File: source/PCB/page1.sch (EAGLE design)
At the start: 25 parts, among them J1 RJ45-MJ88-BX11-RVSL2-3420050P1, J2 CONNECTOR-HEADER-6P-3460650P1, J4 CONNECTOR-HEADER-3P-3460810P1, J5 CONNECTOR-HEADER-2X3P-3460180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, Q1 MOSFET-N-044020001, Q2 MOSFET-N-044020001, Q3 MOSFET-N-044020001, Q4 MOSFET-N-044020001, U1 ATMEGA328P-AU-1030060P1, U2 L298-1420010P1

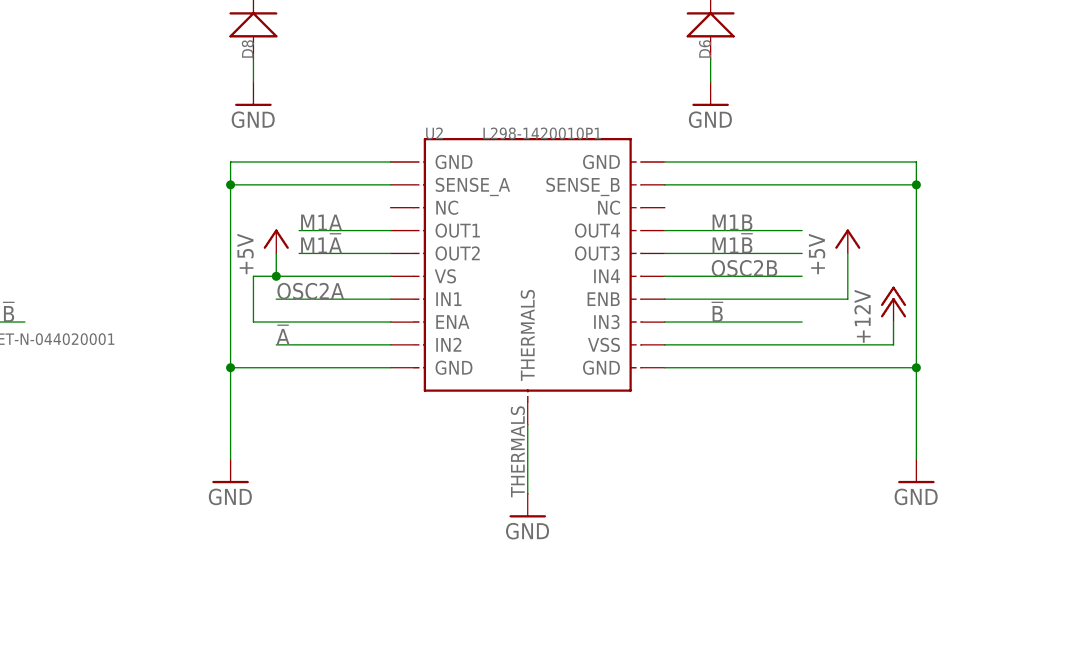
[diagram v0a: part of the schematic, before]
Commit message: LED board update rev3.  Vs and Vss corrected
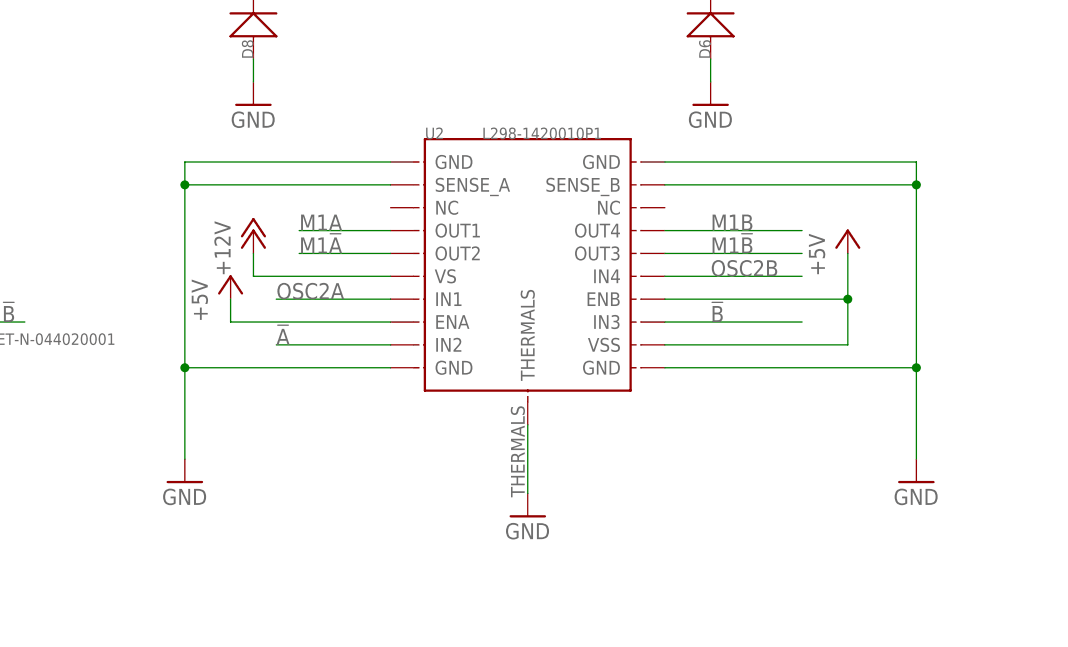
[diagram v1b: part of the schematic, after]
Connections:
- net +12V: now also U2.VS; no longer U2.VSS
- net +5V: now also U2.VSS; no longer U2.VS
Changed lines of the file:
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@@
 <?xml version="1.0" encoding="utf-8"?>
 <!DOCTYPE eagle SYSTEM "eagle.dtd">
-<eagle version="6.5.0">
+<eagle version="7.0.0">
 <drawing>
 <settings>
@@
 <instance part="P+5" gate="1" x="167.64" y="76.2"/>
 <instance part="GND10" gate="1" x="167.64" y="55.88"/>
-<instance part="P+6" gate="1" x="302.26" y="20.32"/>
+<instance part="P+6" gate="1" x="231.14" y="27.94"/>
 <instance part="U$5" gate="G$1" x="198.12" y="91.44" rot="MR180"/>
 <instance part="U$6" gate="G$1" x="198.12" y="66.04" rot="MR180"/>
@@
 <instance part="P+8" gate="1" x="190.5" y="38.1"/>
 <instance part="U2" gate="U" x="261.62" y="22.86"/>
-<instance part="GND3" gate="1" x="228.6" y="0"/>
+<instance part="GND3" gate="1" x="223.52" y="0"/>
 <instance part="GND4" gate="1" x="304.8" y="0"/>
-<instance part="P+9" gate="1" x="233.68" y="27.94"/>
+<instance part="P+9" gate="1" x="228.6" y="22.86"/>
 <instance part="J2" gate="J" x="256.54" y="86.36" rot="MR270"/>
 <instance part="GND6" gate="1" x="261.62" y="-3.81"/>
@@
 </segment>
 <segment>
-<pinref part="U2" gate="U" pin="VSS"/>
-<pinref part="P+6" gate="1" pin="+12V"/>
-<wire x1="276.86" y1="15.24" x2="302.26" y2="15.24" width="0.1524" layer="91"/>
-<wire x1="302.26" y1="15.24" x2="302.26" y2="17.78" width="0.1524" layer="91"/>
-</segment>
-<segment>
 <pinref part="D1" gate="D" pin="-"/>
 <pinref part="P+12" gate="1" pin="+12V"/>
@@
 <junction x="347.98" y="91.44"/>
 <pinref part="P+16" gate="1" pin="+12V"/>
+</segment>
+<segment>
+<pinref part="P+6" gate="1" pin="+12V"/>
+<wire x1="231.14" y1="25.4" x2="231.14" y2="22.86" width="0.1524" layer="91"/>
+<pinref part="U2" gate="U" pin="VS"/>
+<wire x1="231.14" y1="22.86" x2="246.38" y2="22.86" width="0.1524" layer="91"/>
 </segment>
 </net>
@@
 <pinref part="U2" gate="U" pin="GND@1"/>
 <pinref part="GND3" gate="1" pin="GND"/>
-<wire x1="246.38" y1="35.56" x2="228.6" y2="35.56" width="0.1524" layer="91"/>
-<wire x1="228.6" y1="35.56" x2="228.6" y2="33.02" width="0.1524" layer="91"/>
+<wire x1="246.38" y1="35.56" x2="223.52" y2="35.56" width="0.1524" layer="91"/>
+<wire x1="223.52" y1="35.56" x2="223.52" y2="33.02" width="0.1524" layer="91"/>
 <pinref part="U2" gate="U" pin="SENSE_A"/>
-<wire x1="228.6" y1="33.02" x2="228.6" y2="12.7" width="0.1524" layer="91"/>
-<wire x1="228.6" y1="12.7" x2="228.6" y2="2.54" width="0.1524" layer="91"/>
-<wire x1="246.38" y1="33.02" x2="228.6" y2="33.02" width="0.1524" layer="91"/>
+<wire x1="223.52" y1="33.02" x2="223.52" y2="12.7" width="0.1524" layer="91"/>
+<wire x1="223.52" y1="12.7" x2="223.52" y2="2.54" width="0.1524" layer="91"/>
+<wire x1="246.38" y1="33.02" x2="223.52" y2="33.02" width="0.1524" layer="91"/>
 <pinref part="U2" gate="U" pin="GND@10"/>
-<wire x1="246.38" y1="12.7" x2="228.6" y2="12.7" width="0.1524" layer="91"/>
-<junction x="228.6" y="33.02"/>
-<junction x="228.6" y="12.7"/>
+<wire x1="246.38" y1="12.7" x2="223.52" y2="12.7" width="0.1524" layer="91"/>
+<junction x="223.52" y="33.02"/>
+<junction x="223.52" y="12.7"/>
 </segment>
 <segment>
@@
 </segment>
 <segment>
-<pinref part="U2" gate="U" pin="VS"/>
-<pinref part="P+9" gate="1" pin="+5V"/>
-<wire x1="246.38" y1="22.86" x2="233.68" y2="22.86" width="0.1524" layer="91"/>
-<wire x1="233.68" y1="22.86" x2="233.68" y2="25.4" width="0.1524" layer="91"/>
-<pinref part="U2" gate="U" pin="ENA"/>
-<wire x1="246.38" y1="17.78" x2="231.14" y2="17.78" width="0.1524" layer="91"/>
-<wire x1="231.14" y1="17.78" x2="231.14" y2="22.86" width="0.1524" layer="91"/>
-<wire x1="231.14" y1="22.86" x2="233.68" y2="22.86" width="0.1524" layer="91"/>
-<junction x="233.68" y="22.86"/>
-</segment>
-<segment>
 <pinref part="J1" gate="RJ" pin="G+"/>
 <pinref part="P+10" gate="1" pin="+5V"/>
@@
 <pinref part="P+17" gate="1" pin="+5V"/>
 <wire x1="297.18" y1="20.32" x2="297.18" y2="25.4" width="0.1524" layer="91"/>
+<pinref part="U2" gate="U" pin="VSS"/>
+<wire x1="276.86" y1="15.24" x2="297.18" y2="15.24" width="0.1524" layer="91"/>
+<wire x1="297.18" y1="20.32" x2="297.18" y2="15.24" width="0.1524" layer="91"/>
+<junction x="297.18" y="20.32"/>
+</segment>
+<segment>
+<pinref part="U2" gate="U" pin="ENA"/>
+<wire x1="246.38" y1="17.78" x2="228.6" y2="17.78" width="0.1524" layer="91"/>
+<wire x1="228.6" y1="17.78" x2="228.6" y2="20.32" width="0.1524" layer="91"/>
+<pinref part="P+9" gate="1" pin="+5V"/>
 </segment>
 </net>

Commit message: added control over stirrer driver OE
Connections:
- new net MOTOR_EN: U1.PD6(AIN0), U2.ENA, U2.ENB
- net +5V: no longer U2.ENA, U2.ENB
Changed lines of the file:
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@@
 <part name="GND3" library="supply1" deviceset="GND" device=""/>
 <part name="GND4" library="supply1" deviceset="GND" device=""/>
-<part name="P+9" library="supply1" deviceset="+5V" device=""/>
 <part name="J2" library="OPL Eagle Library" deviceset="CONNECTOR-HEADER-6P" device="-3460650P1"/>
 <part name="GND6" library="supply1" deviceset="GND" device=""/>
@@
 <instance part="GND3" gate="1" x="223.52" y="0"/>
 <instance part="GND4" gate="1" x="304.8" y="0"/>
-<instance part="P+9" gate="1" x="228.6" y="22.86"/>
 <instance part="J2" gate="J" x="256.54" y="86.36" rot="MR270"/>
 <instance part="GND6" gate="1" x="261.62" y="-3.81"/>
@@
 </segment>
 <segment>
-<pinref part="U2" gate="U" pin="ENB"/>
-<wire x1="276.86" y1="20.32" x2="297.18" y2="20.32" width="0.1524" layer="91"/>
 <pinref part="P+17" gate="1" pin="+5V"/>
-<wire x1="297.18" y1="20.32" x2="297.18" y2="25.4" width="0.1524" layer="91"/>
 <pinref part="U2" gate="U" pin="VSS"/>
 <wire x1="276.86" y1="15.24" x2="297.18" y2="15.24" width="0.1524" layer="91"/>
-<wire x1="297.18" y1="20.32" x2="297.18" y2="15.24" width="0.1524" layer="91"/>
-<junction x="297.18" y="20.32"/>
-</segment>
-<segment>
-<pinref part="U2" gate="U" pin="ENA"/>
-<wire x1="246.38" y1="17.78" x2="228.6" y2="17.78" width="0.1524" layer="91"/>
-<wire x1="228.6" y1="17.78" x2="228.6" y2="20.32" width="0.1524" layer="91"/>
-<pinref part="P+9" gate="1" pin="+5V"/>
+<wire x1="297.18" y1="25.4" x2="297.18" y2="15.24" width="0.1524" layer="91"/>
 </segment>
 </net>
@@
 </segment>
 </net>
+<net name="MOTOR_EN" class="1">
+<segment>
+<pinref part="U2" gate="U" pin="ENA"/>
+<wire x1="246.38" y1="17.78" x2="228.6" y2="17.78" width="0.1524" layer="91"/>
+<label x="228.6" y="17.78" size="1.778" layer="95"/>
+</segment>
+<segment>
+<pinref part="U2" gate="U" pin="ENB"/>
+<wire x1="276.86" y1="20.32" x2="292.1" y2="20.32" width="0.1524" layer="91"/>
+<label x="279.4" y="20.32" size="1.778" layer="95"/>
+</segment>
+<segment>
+<pinref part="U1" gate="U" pin="PD6(AIN0)"/>
+<wire x1="121.92" y1="40.64" x2="132.08" y2="40.64" width="0.1524" layer="91"/>
+<label x="124.46" y="40.64" size="1.778" layer="95"/>
+</segment>
+</net>

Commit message: updated PCB
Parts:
- removed D1, D2, D3, D4, D5, D6, D7, D8: (no value), OPL Eagle Library:D-SMA
- removed Q1, Q2: MOSFET-N-044020001, OPL Eagle Library:MOSFET-N-044020001
- added C2, C3: 100nf, Seeed-OPL-Capacitor:CERAMIC-100NF-50V-10%-X7R(0805)
- added C4: 220nf, Seeed-OPL-Capacitor:CERAMIC-220NF-25V-10%-X7R(0603)
- added CT1: 100uf, Seeed-OPL-Capacitor:ALUMINUM-SMD-100UF-50V(D8-H10.5MM)
- added R1: 0.2R 1/3W, Seeed-OPL-Resistor:SMD-RES-0.2R-1%-1/3W(0805)
- added R5: 2.7K, Seeed-OPL-Resistor:SMD-RES-2.7K-1%-1/8W(0805)
- added R6: 270R, Seeed-OPL-Resistor:SMD-RES-270R-5%-1/8W(0805)
- J1: value RJ45-MJ88-BX11-RVSL2-3420050P1 -> MJ88-BX11-RVSL2; device OPL Eagle Library:RJ45-MJ88-BX11-RVSL2-3420050P1 -> Seeed-OPL-Connector:RJ45-MJ88-BX11-RVSL2
- R2: value 10k -> 0.2R 1/3W; device OPL Eagle Library:R-0603 -> Seeed-OPL-Resistor:SMD-RES-0.2R-1%-1/3W(0805)
- R4: value 10k -> 22K; device OPL Eagle Library:R-0603 -> Seeed-OPL-Resistor:SMD-RES-22K-5%-1/8W(0805)
- U2: value L298-1420010P1 -> A4988SETTR-QFN28; device OPL Eagle Library:L298-1420010P1 -> Seeed-OPL-ic:DRIVER-A4988SETTR-T(QFN28)
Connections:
- removed net !A: Q1.D, R2.2, U2.IN2
- removed net !B: Q2.D, R4.2, U2.IN3
- removed net M1!A: D7.+, D8.-, J2.3, U2.OUT2
- removed net M1!B: D3.+, D4.-, J2.5, J2.6, U2.OUT3
- removed net MOTOR_EN: U1.PD6(AIN0), U2.ENA, U2.ENB
- removed net OSC2A: Q1.G, R3.2, U1.PB3(MOSI/OC2), U2.IN1
- removed net OSC2B: Q2.G, U1.PD3(INT1), U2.IN4
- new net M!EN: U1.PD6(AIN0), U2.!ENABLE
- new net M!RST: U1.PD2(INT0), U2.!RESET
- new net M!SLP: U1.PB0(ICP), U2.!SLEEP
- new net M2A: J2.4, U2.OUT2A
- new net M2B: J2.5, J2.6, U2.OUT2B
- new net MDIR: U1.PD7(AIN1), U2.DIR
- new net MS1: U1.PC0(ADC0), U2.MS1
- new net MS2: U1.PC1(ADC1), U2.MS2
- new net MS3: U1.PC2(ADC2), U2.MS3
- new net N$10: R4.1, R5.2, U2.REF
- new net N$11: J4.3, R6.2
- new net N$2: R2.1, U2.SENSE1
- new net N$5: R1.1, U2.SENSE2
- new net N$6: C4.2, U2.VREG
- new net N$7: C2.1, U2.CP2
- new net N$8: C2.2, U2.CP1
- new net N$9: C3.1, U2.VCP
- new net OC2A: R3.2, U1.PB3(MOSI/OC2)
- new net OC2B: U1.PD3(INT1), U2.STEP
- net +12V: now also C3.2, CT1.+, U2.VBB1, U2.VBB2; no longer D1.-, D3.-, D5.-, D7.-, U2.VS
- net +5V: now also R4.2, U2.ROSC, U2.VDD; no longer R2.1, R4.1, U2.VSS
- net GND: now also C4.1, CT1.-, R1.2, R2.2, R5.1, U2.GND, U2.PAD; no longer D2.+, D4.+, D6.+, D8.+, Q1.S, Q2.S, U2.GND@10, U2.GND@11, U2.GND@20, U2.SENSE_A, U2.SENSE_B, U2.THERMALS
- net M1A: now also J2.3, U2.OUT1A; no longer D1.+, D2.-, J2.1, J2.2, U2.OUT1
- net M1B: now also J2.1, J2.2, U2.OUT1B; no longer D5.+, D6.-, J2.4, U2.OUT4
- net N$1: now also R6.1
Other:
- moved on the sheet: J1

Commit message: updated pcb with better motor drivers -- tested and working.
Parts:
- removed C3: 100nf, Seeed-OPL-Capacitor:CERAMIC-100NF-50V-10%-X7R(0805)
- removed C4: 220nf, Seeed-OPL-Capacitor:CERAMIC-220NF-25V-10%-X7R(0603)
- removed CT1: 100uf, Seeed-OPL-Capacitor:ALUMINUM-SMD-100UF-50V(D8-H10.5MM)
- removed J2: CONNECTOR-HEADER-6P-3460650P1, OPL Eagle Library:CONNECTOR-HEADER-6P-3460650P1
- removed R1, R2: 0.2R 1/3W, Seeed-OPL-Resistor:SMD-RES-0.2R-1%-1/3W(0805)
- removed R4: 22K, Seeed-OPL-Resistor:SMD-RES-22K-5%-1/8W(0805)
- removed R5: 2.7K, Seeed-OPL-Resistor:SMD-RES-2.7K-1%-1/8W(0805)
- removed U2: A4988SETTR-QFN28, Seeed-OPL-ic:DRIVER-A4988SETTR-T(QFN28)
- added J3: 4p-2.54, Seeed-Connector -2016:DIP-BLACK-MALE-HEADER-VERT(4P-2.54)
- added U$1: A4988BREAKOUT, RepRapjr:A4988BREAKOUT
- C2: value 100nf -> 47uf; device Seeed-OPL-Capacitor:CERAMIC-100NF-50V-10%-X7R(0805) -> Seeed-Capacitor-2016:TANTALUM-SMD-47UF-16V(AVX-C)
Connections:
- removed net GND: C1.1, C4.1, CT1.-, ISP.4, J1.7, J5.1, Q3.S, Q4.S, R1.2, R2.2, R5.1, U$5.GND, U$6.GND, U1.GND, U1.GND@1, U1.GND@2, U2.GND, U2.GND@1, U2.PAD
- removed net M1A: J2.3, U2.OUT1A
- removed net M1B: J2.1, J2.2, U2.OUT1B
- removed net M2A: J2.4, U2.OUT2A
- removed net M2B: J2.5, J2.6, U2.OUT2B
- removed net N$10: R4.1, R5.2, U2.REF
- removed net N$2: R2.1, U2.SENSE1
- removed net N$5: R1.1, U2.SENSE2
- removed net N$6: C4.2, U2.VREG
- removed net N$7: C2.1, U2.CP2
- removed net N$8: C2.2, U2.CP1
- removed net N$9: C3.1, U2.VCP
- new net EEE: C1.1, C2.-, ISP.4, J1.7, J5.1, Q3.S, Q4.S, U$1.GND@0, U$1.GND@1, U$5.GND, U$6.GND, U1.GND, U1.GND@1, U1.GND@2
- new net N$13: J3.P$1, U$1.2B
- new net N$14: J3.P$2, U$1.2A
- new net N$15: J3.P$3, U$1.1A
- new net N$16: J3.P$4, U$1.1B
- net +12V: now also C2.+, U$1.VMOT; no longer C3.2, CT1.+, U2.VBB1, U2.VBB2
- net +5V: now also U$1.VDD; no longer R4.2, U2.ROSC, U2.VDD
- net M!EN: now also U$1.EN; no longer U2.!ENABLE
- net M!RST: now also U$1.RST; no longer U2.!RESET
- net M!SLP: now also U$1.SLEEP; no longer U2.!SLEEP
- net MDIR: now also U$1.DIR; no longer U2.DIR
- net MS1: now also U$1.MS1; no longer U2.MS1
- net MS2: now also U$1.MS2; no longer U2.MS2
- net MS3: now also U$1.MS3; no longer U2.MS3
- net OC2B: now also U$1.STEP; no longer U2.STEP
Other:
- note added: "Set at 400 ma. =160mV for pololu board (Rs=0.05) =320mV for ebay (Rs=0.1)"
